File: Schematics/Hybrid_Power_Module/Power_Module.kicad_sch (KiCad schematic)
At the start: 0 parts

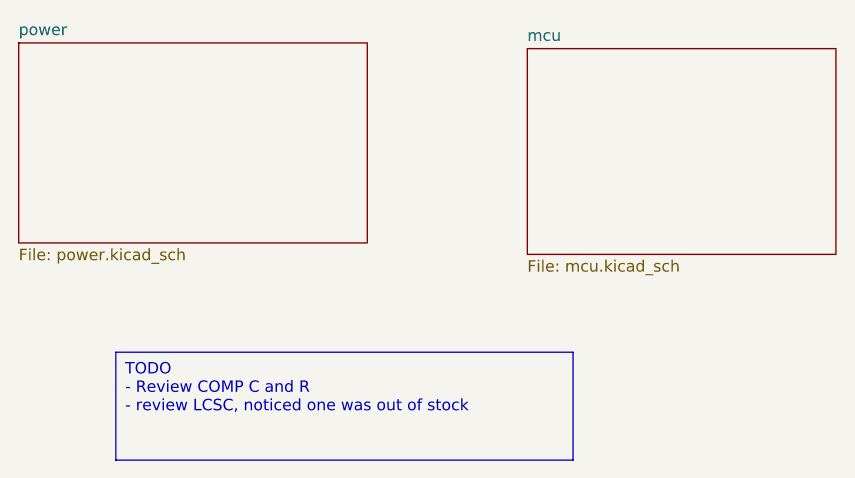
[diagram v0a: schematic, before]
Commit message: finished power board silkscreen, needs final review before approval
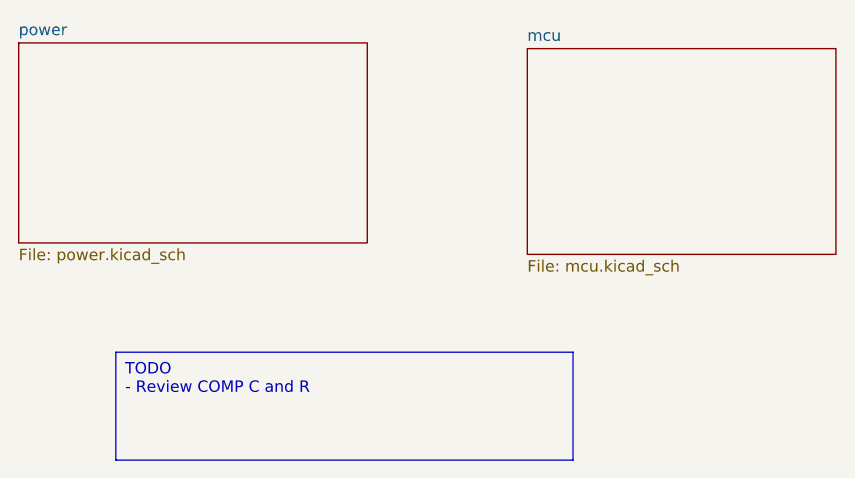
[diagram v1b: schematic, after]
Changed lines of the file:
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@@
 		(comment 4 "GRID = 0.635mm")
 	)
-	(text_box "TODO\n - Review COMP C and R\n - review LCSC, noticed one was out of stock"
+	(text_box "TODO\n - Review COMP C and R"
 		(exclude_from_sim no)
 		(at 113.03 115.0112 0)
